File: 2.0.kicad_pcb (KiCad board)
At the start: 2 copper layers, 38.1 x 50 mm, 26 parts, among them U1 BAT-HLD-001-TR

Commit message: Added OSHW logo
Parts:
- added REF**: OSHW-Logo2_7.3x6mm_SilkScreen, Symbol:OSHW-Logo2_7.3x6mm_SilkScreen, B.Cu at (166.0, 120.3)

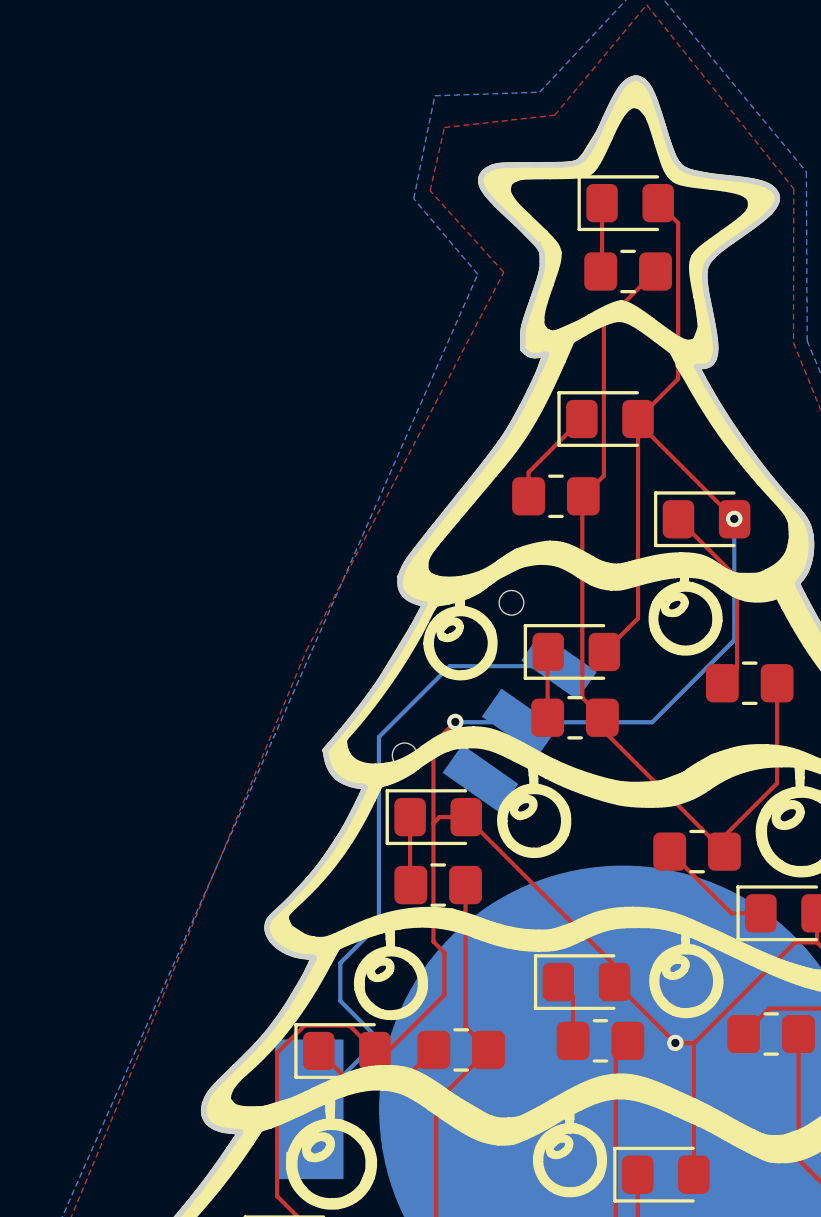
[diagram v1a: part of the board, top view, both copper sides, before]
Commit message: Minor copper changes
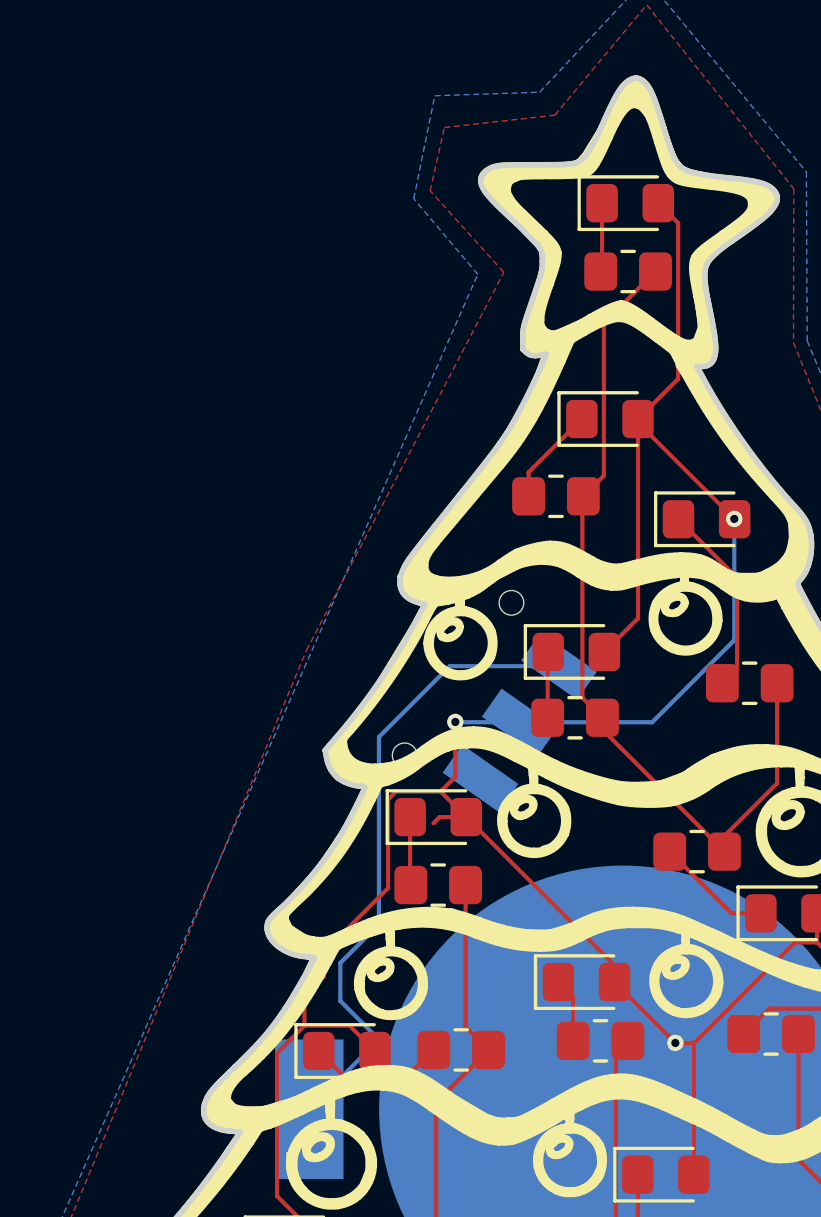
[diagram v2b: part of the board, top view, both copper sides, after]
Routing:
- net Net-(D1-Pad2): track 106.6 -> 108.9 mm
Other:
- board text added: "https://github.com/gjlp25/KiCad_FlashyTree"
- board text removed: "https://github.com/gjlp25"
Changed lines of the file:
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@@
     (tags "LED handsolder")
     (attr smd)
-    (fp_text reference "D8" (at 0 -1.65) (layer "F.SilkS") hide
+    (fp_text reference "D8" (at -0.32764 -1.5772) (layer "F.SilkS") hide
       (effects (font (size 1 1) (thickness 0.15)))
     )
@@
   (gr_poly
     (pts
-      (xy 172.39 108.73)
-      (xy 172.81 109.01)
-      (xy 173.02 109.53)
-      (xy 173.06 110.02)
-      (xy 172.85 110.41)
-      (xy 172.57 110.66)
-      (xy 172.19 110.79)
-      (xy 171.69 110.79)
-      (xy 171.31 110.64)
-      (xy 171.07 110.37)
-      (xy 170.89 109.96)
-      (xy 170.89 109.53)
-      (xy 170.99 109.22)
-      (xy 171.1 109.2)
-      (xy 171.33 109.53)
-      (xy 171.6 109.52)
-      (xy 171.81 109.4)
-      (xy 171.91 109.2)
-      (xy 171.89 109.03)
-      (xy 171.6 108.88)
-      (xy 171.79 108.62)
+      (xy 172.14 108.73)
+      (xy 172.42 108.82)
+      (xy 172.82 109.02)
+      (xy 172.97 109.3)
+      (xy 173.06 109.68)
+      (xy 173.01 110.06)
+      (xy 172.87 110.42)
+      (xy 172.5 110.72)
+      (xy 172.06 110.84)
+      (xy 171.6 110.78)
+      (xy 171.2 110.51)
+      (xy 170.95 110)
+      (xy 170.94 109.58)
+      (xy 171.08 109.22)
+      (xy 171.25 109.33)
+      (xy 171.45 109.56)
+      (xy 171.74 109.48)
+      (xy 171.99 109.21)
+      (xy 171.76 109.02)
+      (xy 171.45 108.94)
+      (xy 171.62 108.77)
+      (xy 171.82 108.69)
     ) (layer "F.Mask") (width 0.1) (fill solid))
   (gr_poly
@@
   (gr_curve (pts (xy 191.872013 106.010584) (xy 191.155844 105.143926) (xy 190.725565 104.38853) (xy 190.329512 103.302818)) (layer "Edge.Cuts") (width 0.2))
   (gr_curve (pts (xy 168.10736 110.6551) (xy 167.567975 111.465305) (xy 167.194638 111.899584) (xy 166.262217 112.801305)) (layer "Edge.Cuts") (width 0.2))
-  (gr_curve (pts (xy 175.237308 80.41131) (xy 175.237308 80.730851) (xy 175.500164 81.051636) (xy 176.536384 81.996835)) (layer "Edge.Cuts") (width 0.2))
+  (gr_curve (pts (xy 175.237308 80.41131) (xy 175.237308 80.730851) (xy 175.500164 81.051636) (xy 176.536384 81.99)) (layer "Edge.Cuts") (width 0.2))
   (gr_curve (pts (xy 195.970399 117.051273) (xy 195.617456 116.596386) (xy 194.994253 115.741377) (xy 195.006584 115.728987)) (layer "Edge.Cuts") (width 0.2))
   (gr_curve (pts (xy 190.410418 102.612711) (xy 190.896911 102.57777) (xy 191.244548 102.457864) (xy 191.461395 102.250089)) (layer "Edge.Cuts") (width 0.2))
@@
   (gr_line (start 173.199375 95.898109) (end 172.916082 96.436575) (layer "Edge.Cuts") (width 0.2))
   (gr_line (start 161.339207 121.000768) (end 161.361247 121.291836) (layer "Edge.Cuts") (width 0.2))
-  (gr_curve (pts (xy 175.70533 79.932355) (xy 175.421781 80.025387) (xy 175.237308 80.214138) (xy 175.237308 80.41131)) (layer "Edge.Cuts") (width 0.2))
+  (gr_curve (pts (xy 175.70533 79.932355) (xy 175.43 80.01) (xy 175.23 80.28) (xy 175.237308 80.41131)) (layer "Edge.Cuts") (width 0.2))
   (gr_curve (pts (xy 198.104622 122.324276) (xy 198.431753 122.344491) (xy 198.514653 122.335944) (xy 198.709028 122.262195)) (layer "Edge.Cuts") (width 0.2))
   (gr_curve (pts (xy 183.658985 122.906113) (xy 184.680322 122.550506) (xy 185.416497 122.579107) (xy 187.309519 123.047874)) (layer "Edge.Cuts") (width 0.2))
@@
     (effects (font (size 1 1) (thickness 0.15)) (justify mirror))
   )
-  (gr_text "https://github.com/gjlp25" (at 185.76 100.02 -67) (layer "B.SilkS")
+  (gr_text "https://github.com/gjlp25/KiCad_FlashyTree" (at 184.51 96.6 -67) (layer "B.SilkS")
     (effects (font (size 0.5 0.5) (thickness 0.125)) (justify mirror))
   )
@@
   (segment (start 190.9445 111.67618) (end 190.9445 114.7645) (width 0.1524) (layer "F.Cu") (net 1))
   (segment (start 183.02108 111.944377) (end 183.02108 116.73332) (width 0.1524) (layer "F.Cu") (net 1))
-  (segment (start 173.51078 103.89922) (end 173.51078 100.99922) (width 0.1524) (layer "F.Cu") (net 1))
   (segment (start 167.8 112.288677) (end 167.8 117.51932) (width 0.1524) (layer "F.Cu") (net 1))
   (segment (start 187.51942 108.2511) (end 186.714357 108.2511) (width 0.1524) (layer "F.Cu") (net 1))
@@
   (segment (start 170.44452 111.28908) (end 168.799597 111.28908) (width 0.1524) (layer "F.Cu") (net 1))
   (segment (start 180.98146 96.41332) (end 180.98146 89.13622) (width 0.1524) (layer "F.Cu") (net 1))
+  (segment (start 168.799597 110.200403) (end 169.5 109.5) (width 0.1524) (layer "F.Cu") (net 1))
+  (segment (start 173.77248 102.74) (end 174.70766 103.67518) (width 0.1524) (layer "F.Cu") (net 1))
   (segment (start 174.70766 103.67518) (end 173.73482 103.67518) (width 0.1524) (layer "F.Cu") (net 1))
-  (segment (start 173.51078 100.99922) (end 174.31 100.2) (width 0.1524) (layer "F.Cu") (net 1))
   (segment (start 184.49658 92.78342) (end 184.50952 92.79636) (width 0.1524) (layer "F.Cu") (net 1))
   (segment (start 182.44752 87.67016) (end 180.98146 89.13622) (width 0.1524) (layer "F.Cu") (net 1))
   (segment (start 183.042729 111.922729) (end 183.02108 111.944377) (width 0.1524) (layer "F.Cu") (net 1))
   (segment (start 187.51942 108.2511) (end 190.9445 111.67618) (width 0.1524) (layer "F.Cu") (net 1))
-  (segment (start 173.91 110.17) (end 171.8628 112.2172) (width 0.1524) (layer "F.Cu") (net 1))
+  (segment (start 171.85454 103.027137) (end 172.141677 102.74) (width 0.1524) (layer "F.Cu") (net 1))
   (segment (start 180.98146 89.13622) (end 180.98146 89.2683) (width 0.1524) (layer "F.Cu") (net 1))
+  (segment (start 168.799597 111.28908) (end 168.799597 110.200403) (width 0.1524) (layer "F.Cu") (net 1))
   (segment (start 187.51942 107.188) (end 187.51942 108.2511) (width 0.1524) (layer "F.Cu") (net 1))
   (segment (start 180.98146 89.2683) (end 184.49658 92.78342) (width 0.1524) (layer "F.Cu") (net 1))
@@
   (segment (start 168.799597 111.28908) (end 167.8 112.288677) (width 0.1524) (layer "F.Cu") (net 1))
   (segment (start 182.44752 81.98152) (end 182.44752 87.67016) (width 0.1524) (layer "F.Cu") (net 1))
-  (segment (start 173.51078 108.22282) (end 173.91 108.62204) (width 0.1524) (layer "F.Cu") (net 1))
+  (segment (start 169.5 108.62) (end 171.85454 106.26546) (width 0.1524) (layer "F.Cu") (net 1))
+  (segment (start 171.85454 106.26546) (end 171.85454 103.027137) (width 0.1524) (layer "F.Cu") (net 1))
   (segment (start 171.37264 112.2172) (end 170.44452 111.28908) (width 0.1524) (layer "F.Cu") (net 1))
+  (segment (start 174.31 102.20248) (end 173.77248 102.74) (width 0.1524) (layer "F.Cu") (net 1))
   (segment (start 167.8 117.51932) (end 169.52098 119.2403) (width 0.1524) (layer "F.Cu") (net 1))
+  (segment (start 169.5 109.5) (end 169.5 108.62) (width 0.1524) (layer "F.Cu") (net 1))
   (segment (start 190.9445 114.7645) (end 194.48526 118.30526) (width 0.1524) (layer "F.Cu") (net 1))
-  (segment (start 173.51078 108.22282) (end 173.51078 103.89922) (width 0.1524) (layer "F.Cu") (net 1))
-  (segment (start 173.91 108.62204) (end 173.91 110.17) (width 0.1524) (layer "F.Cu") (net 1))
+  (segment (start 172.141677 102.74) (end 173.77248 102.74) (width 0.1524) (layer "F.Cu") (net 1))
   (segment (start 180.12294 109.09046) (end 174.70766 103.67518) (width 0.1524) (layer "F.Cu") (net 1))
+  (segment (start 174.31 100.2) (end 174.31 102.20248) (width 0.1524) (layer "F.Cu") (net 1))
   (segment (start 180.12294 109.70006) (end 180.12294 109.09046) (width 0.1524) (layer "F.Cu") (net 1))
   (segment (start 182.345609 111.922729) (end 183.042729 111.922729) (width 0.1524) (layer "F.Cu") (net 1))
